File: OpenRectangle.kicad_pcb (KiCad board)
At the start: 2 copper layers, 339.1 x 141.2 mm, 92 parts, among them J1 USB C Connector, J2 JTAG_TC2030, SW1 Boot, SW10 MX_SW_solder, SW11 MX_SW_HS, SW12 MX_SW_solder, SW13 MX_SW_HS, SW14 MX_SW_HS, SW15 MX_SW_solder, SW16 MX_SW_HS, SW17 MX_SW_solder, SW18 MX_SW_HS, SW19 MX_SW_solder, SW2 MX_SW_HS, SW20 MX_SW_solder, SW21 MX_SW_HS, SW22 MX_SW_HS, SW23 MX_SW_solder, SW24 MX_SW_HS, SW25 MX_SW_solder, SW26 MX_SW_HS, SW27 MX_SW_solder, SW28 MX_SW_HS, SW29 MX_SW_solder, SW3 MX_SW_solder, SW30 MX_SW_solder, SW31 MX_SW_HS, SW32 MX_SW_HS, SW33 MX_SW_solder, SW34 MX_SW_HS, SW35 MX_SW_solder, SW36 MX_SW_HS, SW37 MX_SW_solder, SW38 MX_SW_solder, SW39 MX_SW_HS, SW4 MX_SW_solder, SW40 MX_SW_HS, SW41 MX_SW_solder, SW5 MX_SW_HS, SW6 MX_SW_HS, SW7 MX_SW_solder, SW8 MX_SW_solder, SW9 MX_SW_HS, U1 XC6206, U2 USBLC6-2SC6, U3 RP2040, U4 W25Q128JVS, Y1 12MHz

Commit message: modified OpenRectangle design
Modified OpenRectangle design to make it smaller and change button positions
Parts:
- removed G***: LOGO, LOGO
- removed H1: Logo, qw-logo:qw new logo mask md
- removed H2, H3: MountingHole, MountingHole:MountingHole_2.2mm_M2_ISO14580_Pad
- moved SW16 39.5 mm to (293.1, 34.3), turned to -165 degrees
- moved SW17 39.5 mm to (293.1, 34.3), turned to -165 degrees
- moved SW14 39.5 mm to (264.9, 38.8), turned to -165 degrees
- moved SW15 39.5 mm to (264.9, 38.8), turned to -165 degrees
- moved SW34 38.7 mm to (231.9, 109.1), turned to -165 degrees
- moved SW35 38.7 mm to (231.9, 109.1), turned to -165 degrees
- moved SW40 38.5 mm to (256.9, 113.5), turned to -165 degrees
- moved SW41 38.5 mm to (256.9, 113.5), turned to -165 degrees
- moved H4 38.4 mm to (98.0, 46.3)
- moved SW18 37.6 mm to (322.6, 43.0), turned to -165 degrees
- moved SW19 37.6 mm to (322.6, 43.0), turned to -165 degrees
- moved SW12 36.8 mm to (242.4, 57.2), turned to -165 degrees
- moved SW13 36.8 mm to (242.4, 57.2), turned to -165 degrees
- moved H8 35.0 mm to (305.0, 143.8)
- moved H11 35.0 mm to (92.4, 143.8)
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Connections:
- U3 pad 16: A -> C_DN
- U3 pad 17: C_DN -> A
- U3 pad 29: MS -> Z
- U3 pad 30: Z -> X
- U3 pad 31: LS -> B
- U3 pad 32: X -> MS
- U3 pad 34: Y -> LS
- U3 pad 35: B -> Y
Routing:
- net C_DN: track 248.0 -> 171.5 mm
- net Y: track 171.5 -> 107.4 mm
- net LS: track 198.2 -> 136.6 mm
- net R: track 133.9 -> 75.5 mm
- net MS: track 212.7 -> 163.3 mm
- net DOWN: track 142.4 -> 96.3 mm
- net A: track 201.9 -> 160.8 mm
- net LEFT: track 168.4 -> 129.4 mm
- net C_UP: track 113.6 -> 76.1 mm
- net C_LT: track 170.8 -> 133.3 mm
- net X: track 153.7 -> 121.6 mm
- net RIGHT: track 103.7 -> 77.3 mm, vias 0 -> 2
- net C_RT: track 211.9 -> 185.9 mm
- net Z: track 179.9 -> 154.2 mm
- net B: track 115.6 -> 90.7 mm
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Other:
- board size 339.1 x 141.2 mm -> 282.7 x 136.2 mm

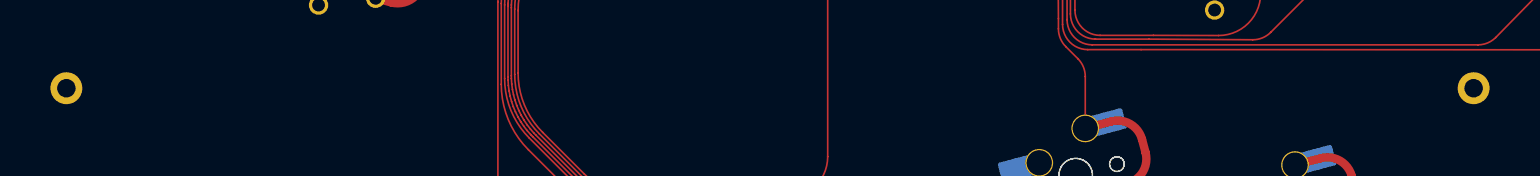
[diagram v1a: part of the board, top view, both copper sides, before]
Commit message: updated case folders
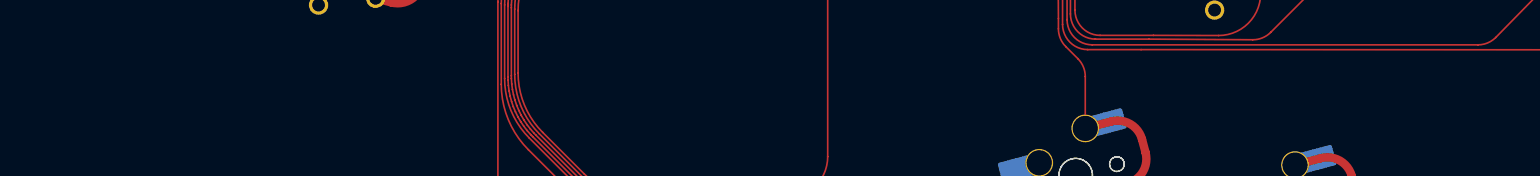
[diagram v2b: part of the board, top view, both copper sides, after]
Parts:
- removed H10, H7: MountingHole, MountingHole:MountingHole_2.2mm_M2_ISO14580_Pad

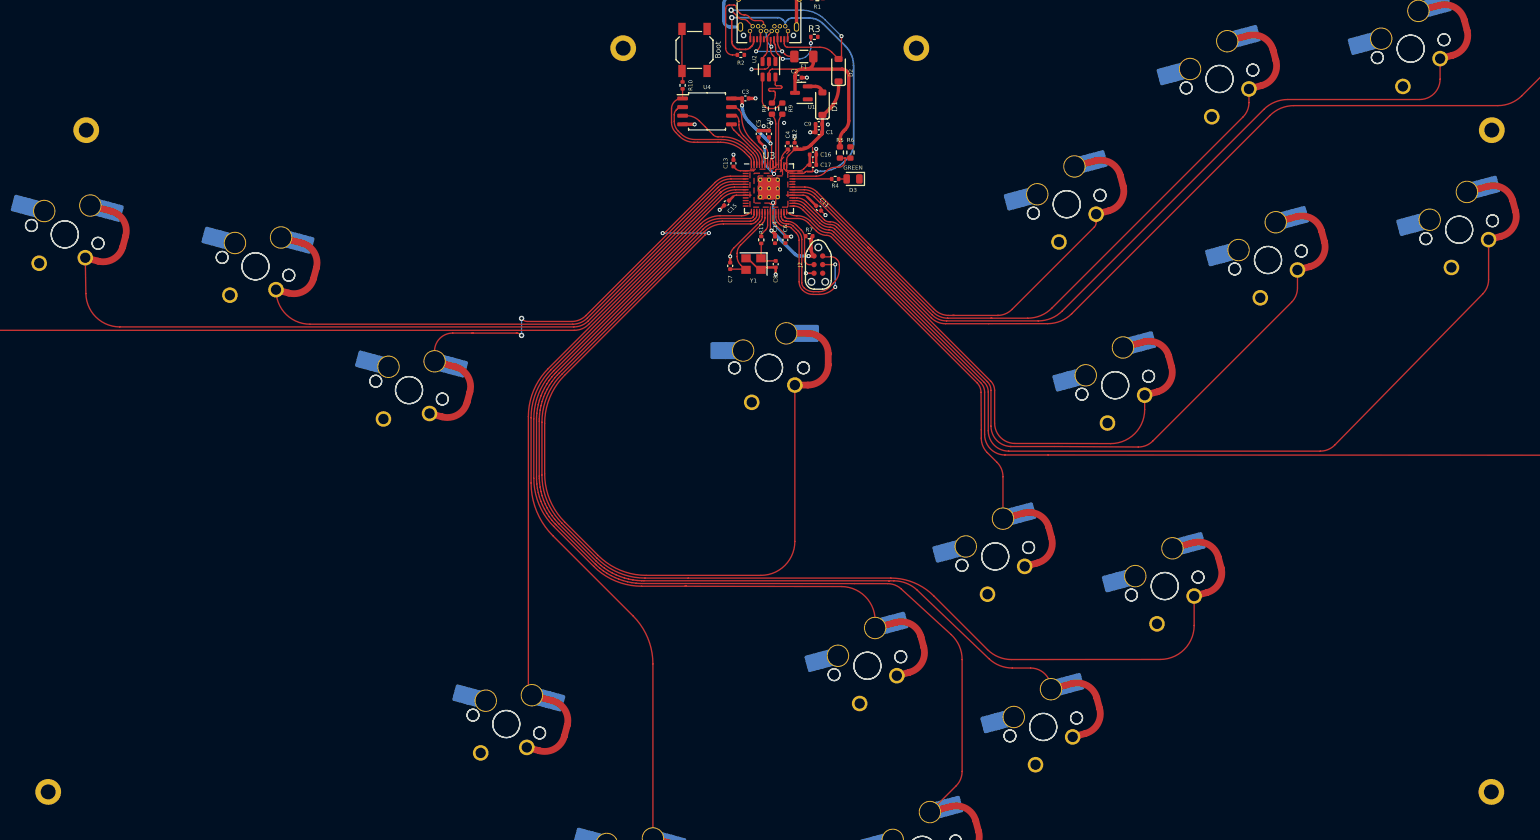
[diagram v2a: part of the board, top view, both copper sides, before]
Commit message: updated mounting hole size
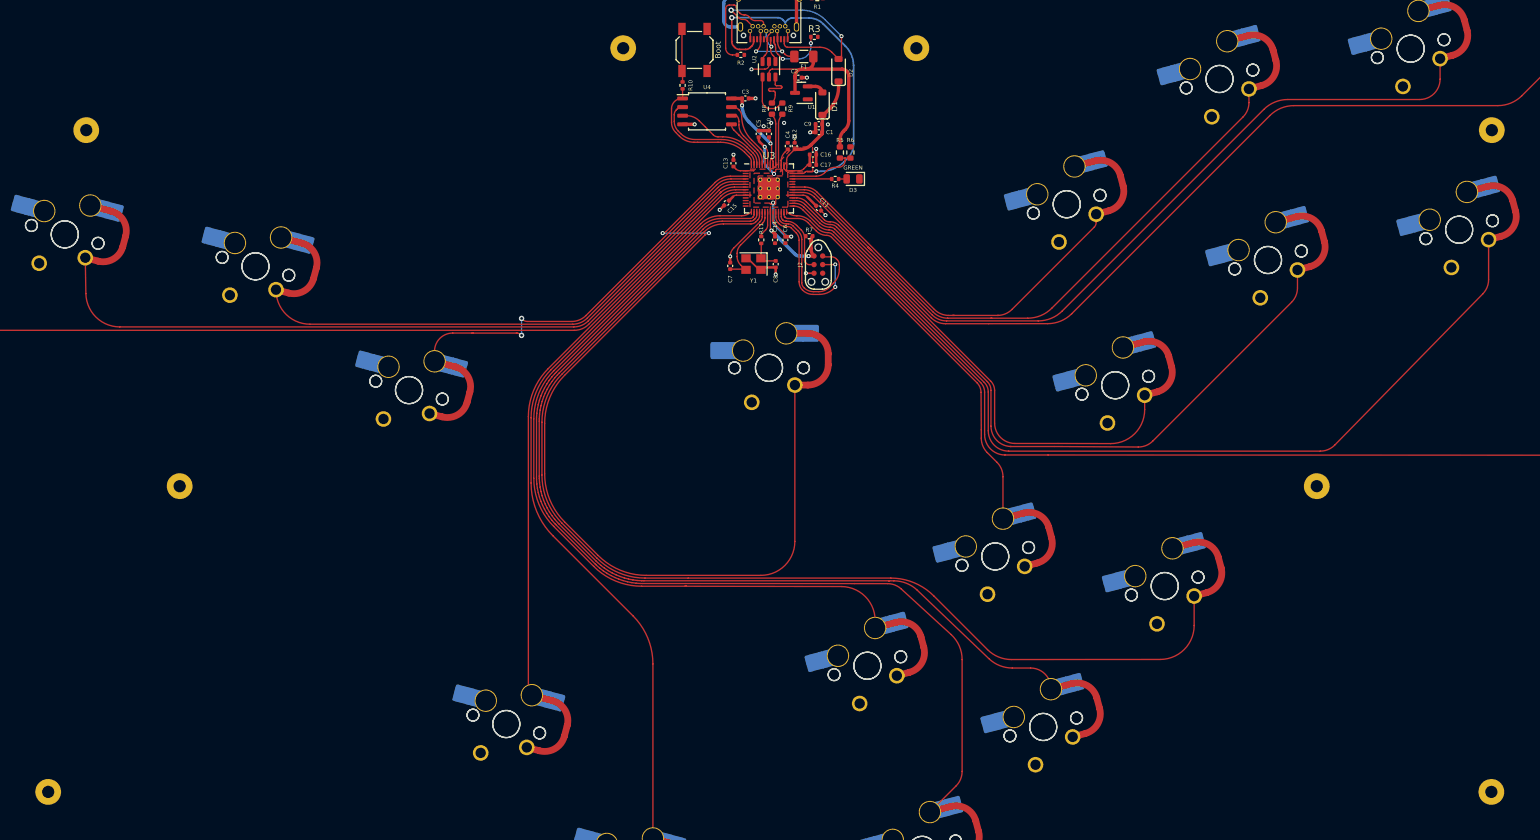
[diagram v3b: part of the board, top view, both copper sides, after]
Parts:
- added H10: MountingHole, MountingHole:MountingHole_2.2mm_M2_ISO14580_Pad, F.Cu at (111.8, 98.8)
- added H7: MountingHole, MountingHole:MountingHole_2.2mm_M2_ISO14580_Pad, F.Cu at (279.3, 98.8)

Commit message: edited case and added annotations to expanded
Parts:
- moved SW12 1.03 mm to (242.7, 58.2)
- moved SW13 1.03 mm to (242.7, 58.2)
- moved SW14 1.03 mm to (265.2, 39.8)
- moved SW15 1.03 mm to (265.2, 39.8)
- moved SW16 1.03 mm to (293.4, 35.3)
- moved SW17 1.03 mm to (293.4, 35.3)
- moved SW18 1.03 mm to (322.8, 44.0)
- moved SW19 1.03 mm to (322.8, 44.0)
- moved H4 1.00 mm to (98.0, 47.3)
- moved H5 1.00 mm to (305.1, 47.3)
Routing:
- net R: track 75.5 -> 76.3 mm
- net Y: track 107.4 -> 106.8 mm

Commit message: updated case
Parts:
- added G***: LOGO, LOGO, B.Cu at (198.4, 94.0)
